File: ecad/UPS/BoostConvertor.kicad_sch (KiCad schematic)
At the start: 17 parts

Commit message: Misc repo cleanup
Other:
- company: (none) -> MTU Open Source Hardware Enterprise
- title: (none) -> Boost Converter
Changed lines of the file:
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@@
 	(generator_version "9.0")
 	(paper "A4")
+	(title_block
+		(title "Boost Converter")
+		(date "2026-02-12")
+		(rev "1.0")
+		(company "MTU Open Source Hardware Enterprise")
+		(comment 1 "Authors: Alex Ritter, Lucas Centner")
+	)
 	(junction
 		(at 137.16 82.55)

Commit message: Updated Symbols
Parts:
- added TP1: 5vTest, symbol Connector:TestPoint
- added TP2: AGNDTest, symbol Connector:TestPoint
- added TP3: PGNDTest, symbol Connector:TestPoint
- C21: value 1pF -> 3900pF
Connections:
- net 5v: now also TP1.1
- net AGND: now also TP2.1
- net PGND: now also TP3.1

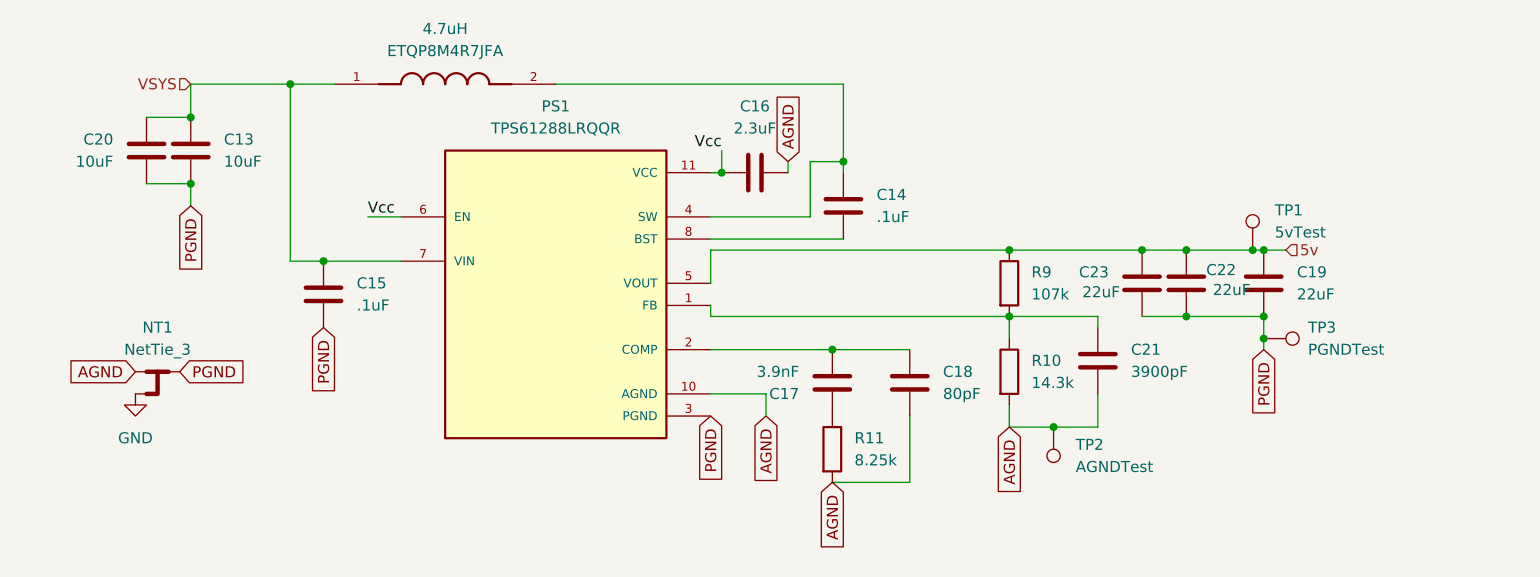
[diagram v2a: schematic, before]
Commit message: Update Symbols and Assign Footprints
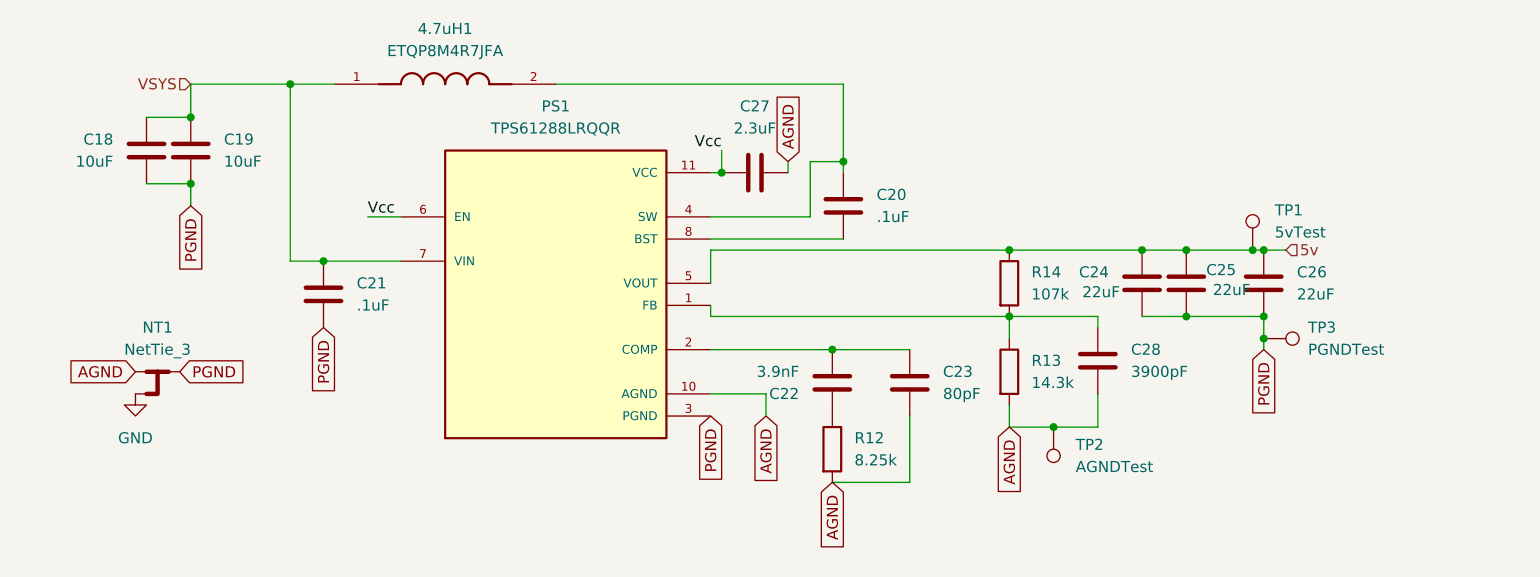
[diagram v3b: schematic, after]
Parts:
- C18: renamed from C20; footprint (none) -> Capacitor_SMD:C_0805_2012Metric_Pad1.18x1.45mm_HandSolder
- C19: renamed from C13; footprint (none) -> Capacitor_SMD:C_0805_2012Metric_Pad1.18x1.45mm_HandSolder
- C20: renamed from C14; footprint (none) -> Capacitor_SMD:C_0402_1005Metric_Pad0.74x0.62mm_HandSolder
- C21: renamed from C15; footprint (none) -> Capacitor_SMD:C_0402_1005Metric_Pad0.74x0.62mm_HandSolder
- C22: renamed from C17; footprint (none) -> Capacitor_SMD:C_0402_1005Metric_Pad0.74x0.62mm_HandSolder
- C23: renamed from C18; footprint (none) -> Capacitor_SMD:C_0402_1005Metric_Pad0.74x0.62mm_HandSolder
- C24: renamed from C23; footprint (none) -> Capacitor_SMD:C_0805_2012Metric_Pad1.18x1.45mm_HandSolder
- C25: renamed from C22; footprint (none) -> Capacitor_SMD:C_0805_2012Metric_Pad1.18x1.45mm_HandSolder
- C26: renamed from C19; footprint (none) -> Capacitor_SMD:C_0805_2012Metric_Pad1.18x1.45mm_HandSolder
- C27: renamed from C16; footprint (none) -> Capacitor_SMD:C_0603_1608Metric_Pad1.08x0.95mm_HandSolder
- C28: renamed from C21; footprint (none) -> Capacitor_SMD:C_0402_1005Metric_Pad0.74x0.62mm_HandSolder
- R12: renamed from R11; footprint (none) -> Capacitor_SMD:C_0603_1608Metric_Pad1.08x0.95mm_HandSolder
- R13: renamed from R10; footprint (none) -> Capacitor_SMD:C_0603_1608Metric_Pad1.08x0.95mm_HandSolder
- R14: renamed from R9; footprint (none) -> Capacitor_SMD:C_0603_1608Metric_Pad1.08x0.95mm_HandSolder
- TP1, TP2, TP3: footprint (none) -> TestPoint:TestPoint_2Pads_Pitch2.54mm_Drill0.8mm
- renumbered 4.7uH to 4.7uH1
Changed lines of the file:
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@@
 		(dnp no)
 		(fields_autoplaced yes)
-		(property "Reference" "C14"
+		(property "Reference" "C20"
 			(at 142.24 64.7699 0)
 			(effects
@@
 			)
 		)
-		(property "Footprint" ""
+		(property "Footprint" "Capacitor_SMD:C_0402_1005Metric_Pad0.74x0.62mm_HandSolder"
 			(at 139.3952 69.85 0)
 			(effects
@@
 			(project ""
 				(path "/9d92b60a-4a6b-449c-b462-cab19e69d38c/66173f08-558e-4192-bd35-ba55c00529e3"
-					(reference "C14")
+					(reference "C20")
 					(unit 1)
 				)
@@
 		(on_board yes)
 		(dnp no)
-		(property "Reference" "R10"
+		(property "Reference" "R13"
 			(at 160.02 83.8199 0)
 			(effects
@@
 			)
 		)
-		(property "Footprint" ""
+		(property "Footprint" "Capacitor_SMD:C_0603_1608Metric_Pad1.08x0.95mm_HandSolder"
 			(at 155.702 85.09 90)
 			(effects
@@
 			(project ""
 				(path "/9d92b60a-4a6b-449c-b462-cab19e69d38c/66173f08-558e-4192-bd35-ba55c00529e3"
-					(reference "R10")
+					(reference "R13")
 					(unit 1)
 				)
@@
 		(on_board yes)
 		(dnp no)
-		(property "Reference" "C20"
+		(property "Reference" "C18"
 			(at 54.61 58.4199 0)
 			(effects
@@
 			)
 		)
-		(property "Footprint" ""
+		(property "Footprint" "Capacitor_SMD:C_0805_2012Metric_Pad1.18x1.45mm_HandSolder"
 			(at 57.4548 63.5 0)
 			(effects
@@
 			(project "UPS"
 				(path "/9d92b60a-4a6b-449c-b462-cab19e69d38c/66173f08-558e-4192-bd35-ba55c00529e3"
-					(reference "C20")
+					(reference "C18")
 					(unit 1)
 				)
@@
 			)
 		)
-		(property "Footprint" ""
+		(property "Footprint" "TestPoint:TestPoint_2Pads_Pitch2.54mm_Drill0.8mm"
 			(at 186.69 86.36 0)
 			(effects
@@
 		(on_board yes)
 		(dnp no)
-		(property "Reference" "C23"
+		(property "Reference" "C24"
 			(at 168.91 73.6599 0)
 			(effects
@@
 			)
 		)
-		(property "Footprint" ""
+		(property "Footprint" "Capacitor_SMD:C_0805_2012Metric_Pad1.18x1.45mm_HandSolder"
 			(at 171.7548 78.74 0)
 			(effects
@@
 			(project "UPS"
 				(path "/9d92b60a-4a6b-449c-b462-cab19e69d38c/66173f08-558e-4192-bd35-ba55c00529e3"
-					(reference "C23")
+					(reference "C24")
 					(unit 1)
 				)
@@
 		(dnp no)
 		(fields_autoplaced yes)
-		(property "Reference" "C18"
+		(property "Reference" "C23"
 			(at 149.86 85.0899 0)
 			(effects
@@
 			)
 		)
-		(property "Footprint" ""
+		(property "Footprint" "Capacitor_SMD:C_0402_1005Metric_Pad0.74x0.62mm_HandSolder"
 			(at 147.0152 90.17 0)
 			(effects
@@
 			(project "UPS"
 				(path "/9d92b60a-4a6b-449c-b462-cab19e69d38c/66173f08-558e-4192-bd35-ba55c00529e3"
-					(reference "C18")
+					(reference "C23")
 					(unit 1)
 				)
@@
 		(dnp no)
 		(fields_autoplaced yes)
-		(property "Reference" "C19"
+		(property "Reference" "C26"
 			(at 190.5 73.6599 0)
 			(effects
@@
 			)
 		)
-		(property "Footprint" ""
+		(property "Footprint" "Capacitor_SMD:C_0805_2012Metric_Pad1.18x1.45mm_HandSolder"
 			(at 187.6552 78.74 0)
 			(effects
@@
 			(project "UPS"
 				(path "/9d92b60a-4a6b-449c-b462-cab19e69d38c/66173f08-558e-4192-bd35-ba55c00529e3"
-					(reference "C19")
+					(reference "C26")
 					(unit 1)
 				)
@@
 		(dnp no)
 		(fields_autoplaced yes)
-		(property "Reference" "C13"
+		(property "Reference" "C19"
 			(at 67.31 58.4199 0)
 			(effects
@@
 			)
 		)
-		(property "Footprint" ""
+		(property "Footprint" "Capacitor_SMD:C_0805_2012Metric_Pad1.18x1.45mm_HandSolder"
 			(at 64.4652 63.5 0)
 			(effects
@@
 			(project ""
 				(path "/9d92b60a-4a6b-449c-b462-cab19e69d38c/66173f08-558e-4192-bd35-ba55c00529e3"
-					(reference "C13")
+					(reference "C19")
 					(unit 1)
 				)
@@
 			)
 		)
-		(property "Footprint" ""
+		(property "Footprint" "TestPoint:TestPoint_2Pads_Pitch2.54mm_Drill0.8mm"
 			(at 157.48 91.44 0)
 			(effects
@@
 		(dnp no)
 		(fields_autoplaced yes)
-		(property "Reference" "#PWR015"
+		(property "Reference" "#PWR0105"
 			(at 57.15 93.98 0)
 			(effects
@@
 			(project "UPS"
 				(path "/9d92b60a-4a6b-449c-b462-cab19e69d38c/66173f08-558e-4192-bd35-ba55c00529e3"
-					(reference "#PWR015")
+					(reference "#PWR0105")
 					(unit 1)
 				)
@@
 		(dnp no)
 		(fields_autoplaced yes)
-		(property "Reference" "C15"
+		(property "Reference" "C21"
 			(at 82.55 74.9299 0)
 			(effects
@@
 			)
 		)
-		(property "Footprint" ""
+		(property "Footprint" "Capacitor_SMD:C_0402_1005Metric_Pad0.74x0.62mm_HandSolder"
 			(at 79.7052 80.01 0)
 			(effects
@@
 			(project "UPS"
 				(path "/9d92b60a-4a6b-449c-b462-cab19e69d38c/66173f08-558e-4192-bd35-ba55c00529e3"
-					(reference "C15")
+					(reference "C21")
 					(unit 1)
 				)
@@
 		(on_board yes)
 		(dnp no)
-		(property "Reference" "R9"
+		(property "Reference" "R14"
 			(at 160.02 73.6599 0)
 			(effects
@@
 			)
 		)
-		(property "Footprint" ""
+		(property "Footprint" "Capacitor_SMD:C_0603_1608Metric_Pad1.08x0.95mm_HandSolder"
 			(at 155.702 74.93 90)
 			(effects
@@
 			(project ""
 				(path "/9d92b60a-4a6b-449c-b462-cab19e69d38c/66173f08-558e-4192-bd35-ba55c00529e3"
-					(reference "R9")
+					(reference "R14")
 					(unit 1)
 				)
@@
 		(dnp no)
 		(fields_autoplaced yes)
-		(property "Reference" "4.7uH"
+		(property "Reference" "4.7uH1"
 			(at 92.71 45.72 0)
 			(effects
@@
 			(project ""
 				(path "/9d92b60a-4a6b-449c-b462-cab19e69d38c/66173f08-558e-4192-bd35-ba55c00529e3"
-					(reference "4.7uH")
+					(reference "4.7uH1")
 					(unit 1)
 				)
@@
 		(dnp no)
 		(fields_autoplaced yes)
-		(property "Reference" "C21"
+		(property "Reference" "C28"
 			(at 171.45 82.5499 0)
 			(effects
@@
 			)
 		)
-		(property "Footprint" ""
+		(property "Footprint" "Capacitor_SMD:C_0402_1005Metric_Pad0.74x0.62mm_HandSolder"
 			(at 168.6052 87.63 0)
 			(effects
@@
 			(project ""
 				(path "/9d92b60a-4a6b-449c-b462-cab19e69d38c/66173f08-558e-4192-bd35-ba55c00529e3"
-					(reference "C21")
+					(reference "C28")
 					(unit 1)
 				)
@@
 		(on_board yes)
 		(dnp no)
-		(property "Reference" "C22"
+		(property "Reference" "C25"
 			(at 180.086 73.406 0)
 			(effects
@@
 			)
 		)
-		(property "Footprint" ""
+		(property "Footprint" "Capacitor_SMD:C_0805_2012Metric_Pad1.18x1.45mm_HandSolder"
 			(at 178.7652 78.74 0)
 			(effects
@@
 			(project "UPS"
 				(path "/9d92b60a-4a6b-449c-b462-cab19e69d38c/66173f08-558e-4192-bd35-ba55c00529e3"
-					(reference "C22")
+					(reference "C25")
 					(unit 1)
 				)
@@
 			)
 		)
-		(property "Footprint" ""
+		(property "Footprint" "TestPoint:TestPoint_2Pads_Pitch2.54mm_Drill0.8mm"
 			(at 190.5 71.12 0)
 			(effects
@@
 		(dnp no)
 		(fields_autoplaced yes)
-		(property "Reference" "R11"
+		(property "Reference" "R12"
 			(at 139.7 92.7099 0)
 			(effects
@@
 			)
 		)
-		(property "Footprint" ""
+		(property "Footprint" "Capacitor_SMD:C_0603_1608Metric_Pad1.08x0.95mm_HandSolder"
 			(at 135.382 93.98 90)
 			(effects
@@
 			(project ""
 				(path "/9d92b60a-4a6b-449c-b462-cab19e69d38c/66173f08-558e-4192-bd35-ba55c00529e3"
-					(reference "R11")
+					(reference "R12")
 					(unit 1)
 				)
@@
 		(on_board yes)
 		(dnp no)
-		(property "Reference" "C17"
+		(property "Reference" "C22"
 			(at 133.35 87.6301 0)
 			(effects
@@
 			)
 		)
-		(property "Footprint" ""
+		(property "Footprint" "Capacitor_SMD:C_0402_1005Metric_Pad0.74x0.62mm_HandSolder"
 			(at 136.1948 82.55 0)
 			(effects
@@
 			(project "UPS"
 				(path "/9d92b60a-4a6b-449c-b462-cab19e69d38c/66173f08-558e-4192-bd35-ba55c00529e3"
-					(reference "C17")
+					(reference "C22")
 					(unit 1)
 				)
@@
 		(dnp no)
 		(fields_autoplaced yes)
-		(property "Reference" "C16"
+		(property "Reference" "C27"
 			(at 128.27 54.61 90)
 			(effects
@@
 			)
 		)
-		(property "Footprint" ""
+		(property "Footprint" "Capacitor_SMD:C_0603_1608Metric_Pad1.08x0.95mm_HandSolder"
 			(at 132.08 61.2648 0)
 			(effects
@@
 			(project "UPS"
 				(path "/9d92b60a-4a6b-449c-b462-cab19e69d38c/66173f08-558e-4192-bd35-ba55c00529e3"
-					(reference "C16")
-					(unit 1)
-				)
+					(reference "C27")
+					(unit 1)
+				)

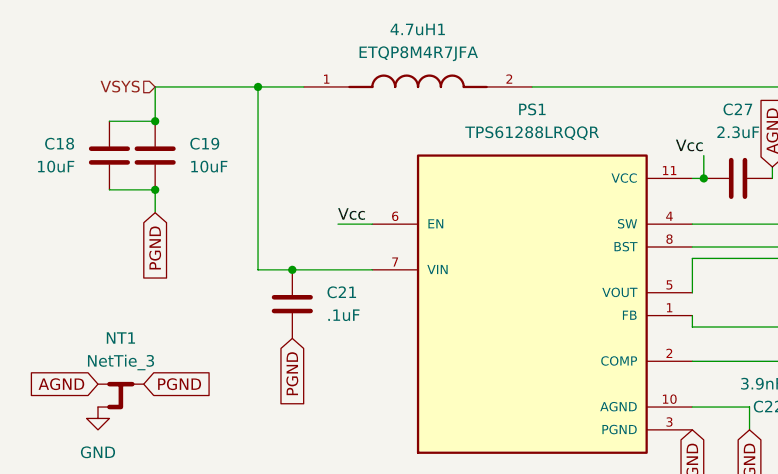
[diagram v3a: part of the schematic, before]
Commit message: added testpoint
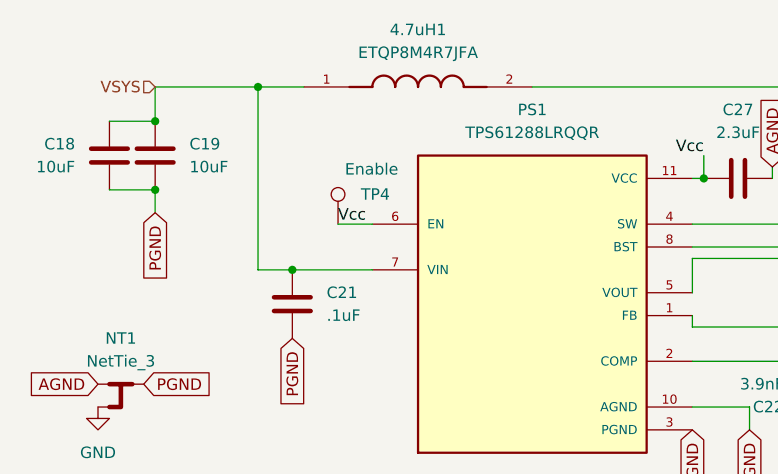
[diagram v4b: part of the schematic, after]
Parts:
- added TP4: Enable, TestPoint:TestPoint_2Pads_Pitch2.54mm_Drill0.8mm, symbol Connector:TestPoint
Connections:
- net Vcc: now also TP4.1
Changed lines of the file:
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@@
+	)
+	(symbol
+		(lib_id "Connector:TestPoint")
+		(at 83.82 67.31 0)
+		(unit 1)
+		(exclude_from_sim no)
+		(in_bom yes)
+		(on_board yes)
+		(dnp no)
+		(property "Reference" "TP4"
+			(at 86.36 64.0079 0)
+			(effects
+				(font
+					(size 1.27 1.27)
+				)
+				(justify left)
+			)
+		)
+		(property "Value" "Enable"
+			(at 84.582 61.214 0)
+			(do_not_autoplace yes)
+			(effects
+				(font
+					(size 1.27 1.27)
+				)
+				(justify left)
+			)
+		)
+		(property "Footprint" "TestPoint:TestPoint_2Pads_Pitch2.54mm_Drill0.8mm"
+			(at 88.9 67.31 0)
+			(effects
+				(font
+					(size 1.27 1.27)
+				)
+				(hide yes)
+			)
+		)
+		(property "Datasheet" "~"
+			(at 88.9 67.31 0)
+			(effects
+				(font
+					(size 1.27 1.27)
+				)
+				(hide yes)
+			)
+		)
+		(property "Description" "test point"
+			(at 83.82 67.31 0)
+			(effects
+				(font
+					(size 1.27 1.27)
+				)
+				(hide yes)
+			)
+		)
+		(pin "1"
+		)
+		(instances
+			(project "UPS"
+				(path "/9d92b60a-4a6b-449c-b462-cab19e69d38c/66173f08-558e-4192-bd35-ba55c00529e3"
+					(reference "TP4")
+					(unit 1)
+				)
+			)
+		)
 	)
 	(symbol

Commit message: assign footprints
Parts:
- added C3: .1uF, Capacitor_SMD:C_0402_1005Metric_Pad0.74x0.62mm_HandSolder, symbol Device:C
- added JP1: SolderJumper_2_Open, Jumper:SolderJumper-2_P1.3mm_Open_Pad1.0x1.5mm, symbol Jumper:SolderJumper_2_Open
- added TP5: Vin, UPS:TespointBig, symbol Connector:TestPoint
- C27: value 2.3uF -> 2.2uF
- C28: value 3900pF -> 1pF
- TP1, TP2, TP4: footprint TestPoint:TestPoint_2Pads_Pitch2.54mm_Drill0.8mm -> TestPoint:TestPoint_Pad_D1.5mm
- TP3: footprint TestPoint:TestPoint_2Pads_Pitch2.54mm_Drill0.8mm -> UPS:TespointBig
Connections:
- net 5v: now also C3.1
- net PGND: now also C3.2
- net VSYS: now also JP1.1 (A); no longer 4.7uH1.1, C18.1, C19.1, C21.1, PS1.7 (VIN)
- new net: 4.7uH1.1, C18.1, C19.1, C21.1, JP1.2 (B), PS1.7 (VIN), TP5.1
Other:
- moved on the sheet: C24, C25, C26, TP1, TP3

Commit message: Fix duplicate component names.
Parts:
- removed C27: 2.2uF, Capacitor_SMD:C_0603_1608Metric_Pad1.08x0.95mm_HandSolder, symbol Device:C
- removed C28: 1pF, Capacitor_SMD:C_0402_1005Metric_Pad0.74x0.62mm_HandSolder, symbol Device:C
- removed R12: 8.25k, Capacitor_SMD:C_0603_1608Metric_Pad1.08x0.95mm_HandSolder, symbol Device:R
- removed R13: 14.3k, Capacitor_SMD:C_0603_1608Metric_Pad1.08x0.95mm_HandSolder, symbol Device:R
- removed R14: 107k, Capacitor_SMD:C_0603_1608Metric_Pad1.08x0.95mm_HandSolder, symbol Device:R
- added C35: 2.2uF, Capacitor_SMD:C_0603_1608Metric_Pad1.08x0.95mm_HandSolder, symbol Device:C
- added C36: 1pF, Capacitor_SMD:C_0402_1005Metric_Pad0.74x0.62mm_HandSolder, symbol Device:C
- added R30: 8.25k, Capacitor_SMD:C_0603_1608Metric_Pad1.08x0.95mm_HandSolder, symbol Device:R
- added R31: 14.3k, Capacitor_SMD:C_0603_1608Metric_Pad1.08x0.95mm_HandSolder, symbol Device:R
- added R32: 107k, Capacitor_SMD:C_0603_1608Metric_Pad1.08x0.95mm_HandSolder, symbol Device:R
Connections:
- net 5v: now also R32.1
- net AGND: now also C35.2, C36.2, R30.2, R31.2
- net Vcc: now also C35.1
- net at PS1.1 (FB): now also C36.1, R31.1, R32.2
- net at C22.1: now also R30.1
